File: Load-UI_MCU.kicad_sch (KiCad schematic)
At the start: 30 parts, among them IC1 MSPM0G3519SPMR, IC2 TPS73533DRVT, J1 Conn_01x05_Socket, J10 Conn_01x02_Socket, J11 Conn_01x02_Socket, J15 Conn_01x08_Pin, J8 Conn_01x06_Socket, SW1 SW_Push, SW2 SW_Push, SW3 SW_Push_DPDT

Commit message: Updated schematic and cleaned autosave files
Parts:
- IC1: footprint MSPM03507:QFP50P1200X1200X160-64N -> QFP50P1200X1200X160-64N; symbol MSPM03509-PCB:MSPM0G3507SPMR -> MSPM0G3507SPMR:MSPM0G3507SPMR
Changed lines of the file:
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@@
 	)
 	(symbol
-		(lib_id "MSPM03509-PCB:MSPM0G3507SPMR")
+		(lib_id "MSPM0G3507SPMR:MSPM0G3507SPMR")
 		(at 105.41 81.28 0)
 		(unit 1)
@@
 			)
 		)
-		(property "Footprint" "MSPM03507:QFP50P1200X1200X160-64N"
+		(property "Footprint" "QFP50P1200X1200X160-64N"
 			(at 177.8 143.18 0)
 			(effects

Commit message: Changed NRST button silkscreen
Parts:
- IC1: footprint QFP50P1200X1200X160-64N -> MSPM0SPMR:QFP50P1200X1200X160-64N
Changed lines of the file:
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@@
 			)
 		)
-		(property "Footprint" "QFP50P1200X1200X160-64N"
+		(property "Footprint" "MSPM0SPMR:QFP50P1200X1200X160-64N"
 			(at 177.8 143.18 0)
 			(effects

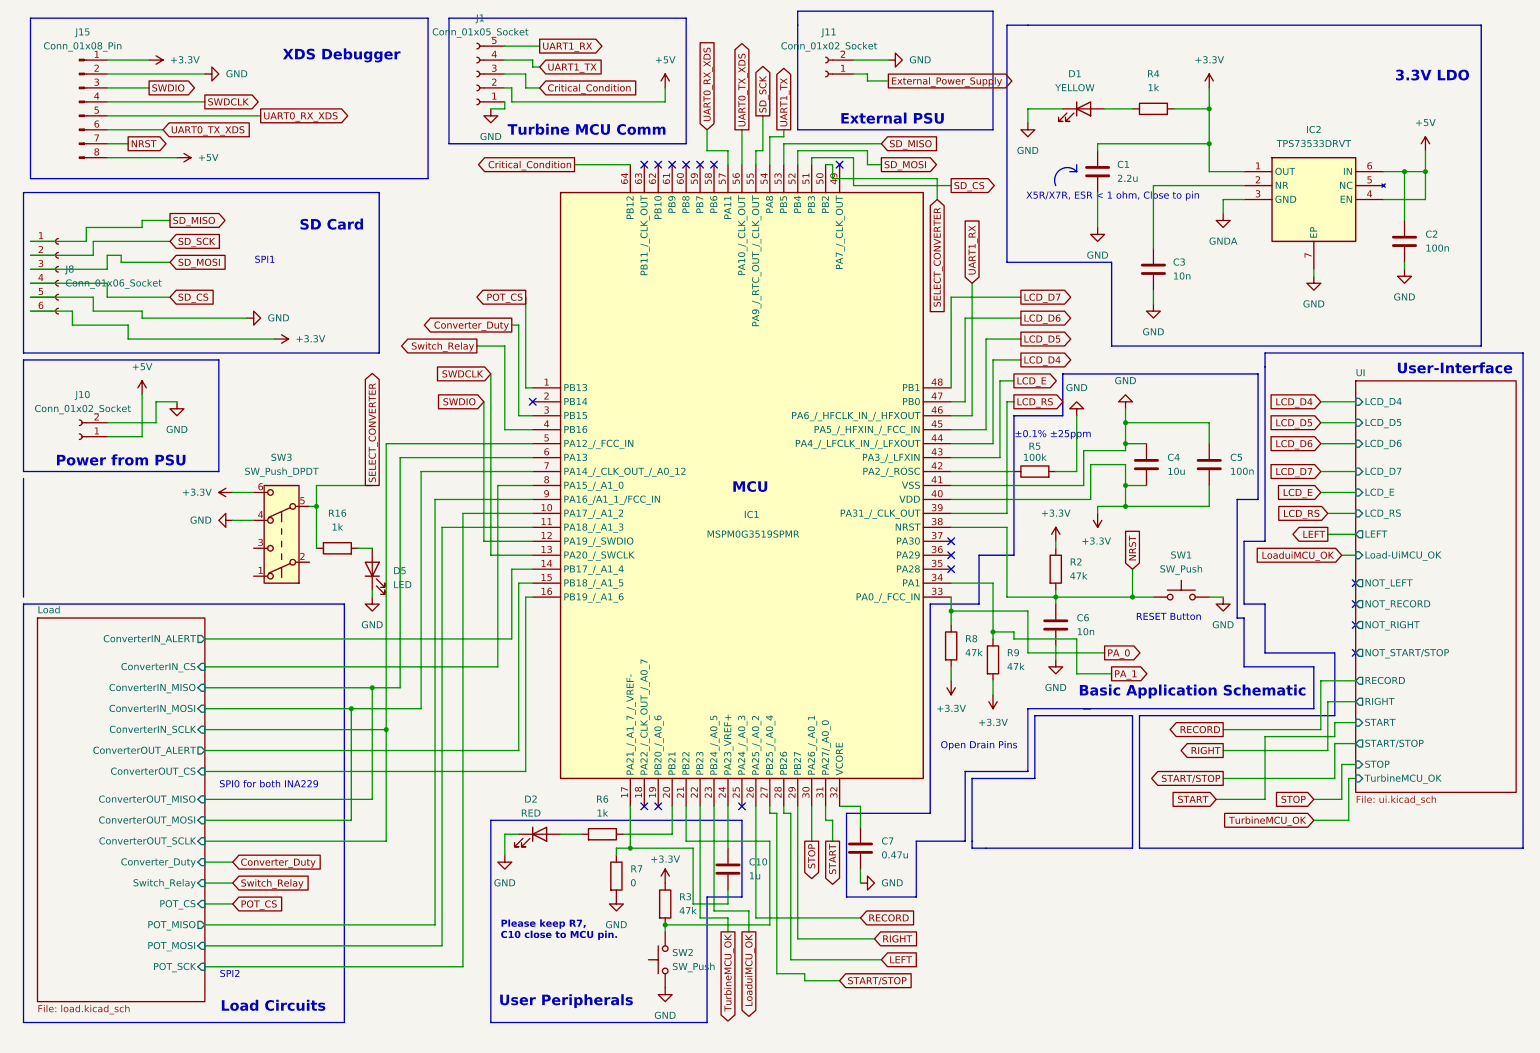
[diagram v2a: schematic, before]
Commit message: Added final changes to PCB: 1. Fixed OV2 ressitors on Power MUX, 2. Added input filtering on both INA229, 3. Changed the LDO layout based on manufacturer recomendations.
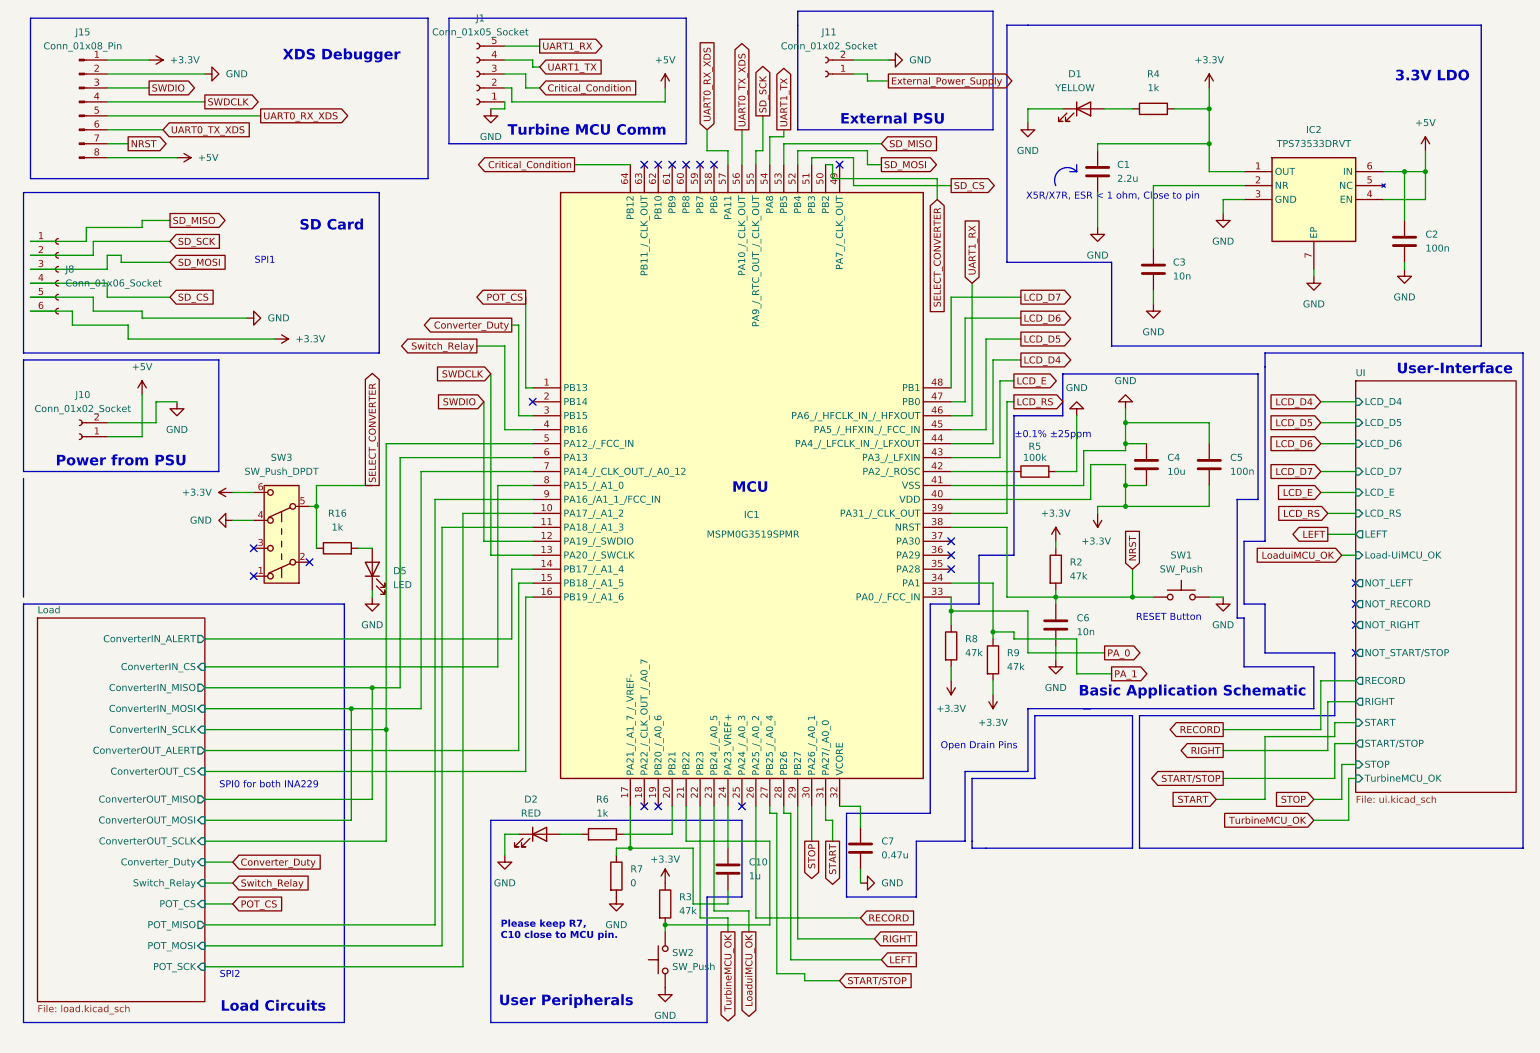
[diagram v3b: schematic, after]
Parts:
- C3: footprint Capacitor_SMD:C_1206_3216Metric_Pad1.33x1.80mm_HandSolder -> Capacitor_SMD:C_0402_1005Metric_Pad0.74x0.62mm_HandSolder
- R4: footprint Resistor_SMD:R_1206_3216Metric_Pad1.30x1.75mm_HandSolder -> Resistor_SMD:R_0805_2012Metric_Pad1.20x1.40mm_HandSolder
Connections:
- net GNDA is gone; now on net GND: IC2.3 (GND)
- no-connect marks 18 -> 21
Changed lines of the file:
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@@
 	)
 	(no_connect
+		(at 54.61 115.57)
+	)
+	(no_connect
 		(at 255.27 120.65)
 	)
 	(no_connect
+		(at 54.61 110.49)
+	)
+	(no_connect
 		(at 255.27 129.54)
 	)
@@
 	)
 	(no_connect
+		(at 64.77 113.03)
+	)
+	(no_connect
 		(at 125.73 40.64)
 	)
@@
 	)
 	(symbol
+		(lib_id "power:GND")
+		(at 231.14 49.53 0)
+		(unit 1)
+		(exclude_from_sim no)
+		(in_bom yes)
+		(on_board yes)
+		(dnp no)
+		(fields_autoplaced yes)
+		(property "Reference" "#PWR03"
+			(at 231.14 55.88 0)
+			(effects
+				(font
+					(size 1.27 1.27)
+				)
+				(hide yes)
+			)
+		)
+		(property "Value" "GND"
+			(at 231.14 54.61 0)
+			(effects
+				(font
+					(size 1.27 1.27)
+				)
+			)
+		)
+		(property "Footprint" ""
+			(at 231.14 49.53 0)
+			(effects
+				(font
+					(size 1.27 1.27)
+				)
+				(hide yes)
+			)
+		)
+		(property "Datasheet" ""
+			(at 231.14 49.53 0)
+			(effects
+				(font
+					(size 1.27 1.27)
+				)
+				(hide yes)
+			)
+		)
+		(property "Description" "Power symbol creates a global label with name \"GND\" , ground"
+			(at 231.14 49.53 0)
+			(effects
+				(font
+					(size 1.27 1.27)
+				)
+				(hide yes)
+			)
+		)
+		(pin "1"
+		)
+		(instances
+			(project "Load-UI_MCU"
+				(path "/526b8b14-d04c-43b9-8d25-bcbd5ccf5c4d"
+					(reference "#PWR03")
+					(unit 1)
+				)
+			)
+		)
+	)
+	(symbol
 		(lib_id "Device:R")
 		(at 218.44 30.48 90)
@@
 			)
 		)
-		(property "Footprint" "Resistor_SMD:R_1206_3216Metric_Pad1.30x1.75mm_HandSolder"
+		(property "Footprint" "Resistor_SMD:R_0805_2012Metric_Pad1.20x1.40mm_HandSolder"
 			(at 218.44 32.258 90)
 			(effects
@@
 	)
 	(symbol
-		(lib_id "power:GNDA")
-		(at 231.14 49.53 0)
-		(unit 1)
-		(exclude_from_sim no)
-		(in_bom yes)
-		(on_board yes)
-		(dnp no)
-		(fields_autoplaced yes)
-		(property "Reference" "#PWR03"
-			(at 231.14 55.88 0)
-			(effects
-				(font
-					(size 1.27 1.27)
-				)
-				(hide yes)
-			)
-		)
-		(property "Value" "GNDA"
-			(at 231.14 54.61 0)
-			(effects
-				(font
-					(size 1.27 1.27)
-				)
-			)
-		)
-		(property "Footprint" ""
-			(at 231.14 49.53 0)
-			(effects
-				(font
-					(size 1.27 1.27)
-				)
-				(hide yes)
-			)
-		)
-		(property "Datasheet" ""
-			(at 231.14 49.53 0)
-			(effects
-				(font
-					(size 1.27 1.27)
-				)
-				(hide yes)
-			)
-		)
-		(property "Description" "Power symbol creates a global label with name \"GNDA\" , analog ground"
-			(at 231.14 49.53 0)
-			(effects
-				(font
-					(size 1.27 1.27)
-				)
-				(hide yes)
-			)
-		)
-		(pin "1"
-		)
-		(instances
-			(project "Load-UI_MCU"
-				(path "/526b8b14-d04c-43b9-8d25-bcbd5ccf5c4d"
-					(reference "#PWR03")
-					(unit 1)
-				)
-			)
-		)
-	)
-	(symbol
 		(lib_id "power:GND")
 		(at 200.66 130.81 0)
@@
 			)
 		)
-		(property "Footprint" "Capacitor_SMD:C_1206_3216Metric_Pad1.33x1.80mm_HandSolder"
+		(property "Footprint" "Capacitor_SMD:C_0402_1005Metric_Pad0.74x0.62mm_HandSolder"
 			(at 219.4052 63.5 0)
 			(effects
@@
 			)
 		)
-		(pin "ConverterIN_MISO" input
+		(pin "ConverterIN_MISO" output
 			(at 45.72 135.89 0)
 			(effects
@@
 			)
 		)
-		(pin "ConverterOUT_MISO" input
+		(pin "ConverterOUT_MISO" output
 			(at 45.72 156.21 0)
 			(effects

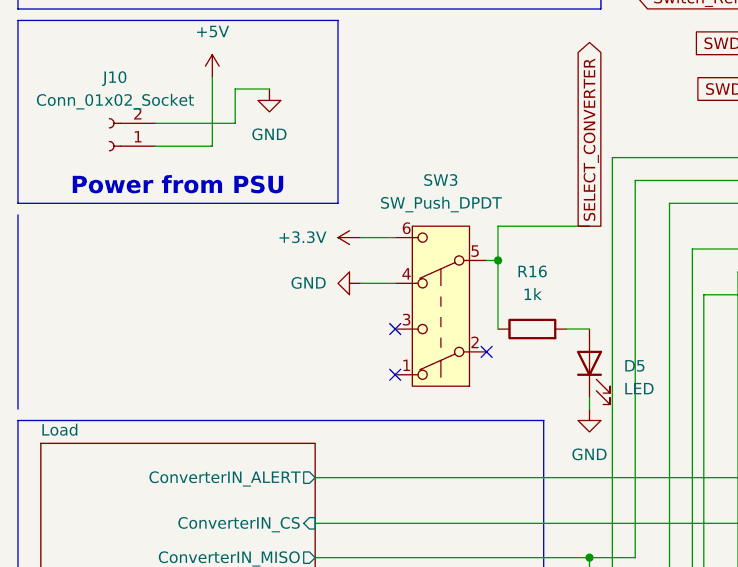
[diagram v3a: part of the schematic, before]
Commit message: Finished pcb for manufacturing, changed some footprints based on what the manufacturer had. Also I fixed the potentiometer footprint.
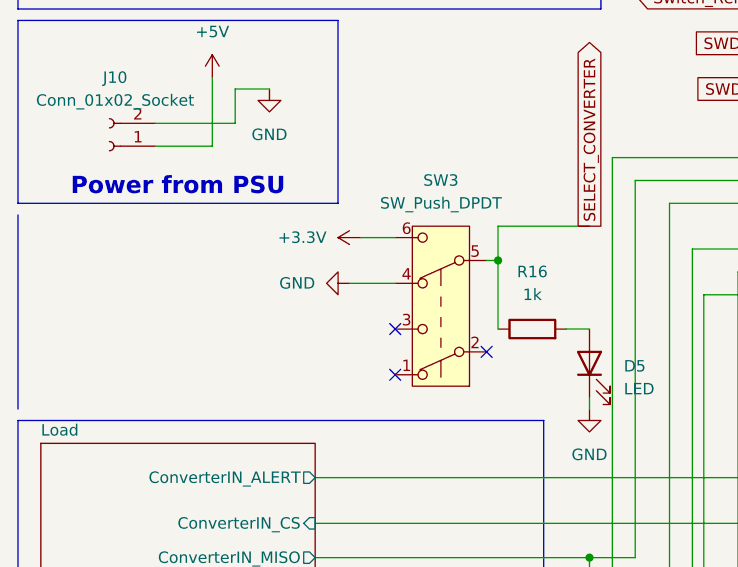
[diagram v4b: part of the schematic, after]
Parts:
- C10: footprint Capacitor_SMD:C_1206_3216Metric_Pad1.33x1.80mm_HandSolder -> Capacitor_SMD:C_0402_1005Metric_Pad0.74x0.62mm_HandSolder
- R7: footprint Resistor_THT:R_Axial_DIN0207_L6.3mm_D2.5mm_P7.62mm_Horizontal -> Resistor_SMD:R_0402_1005Metric_Pad0.72x0.64mm_HandSolder
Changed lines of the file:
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@@
 	(wire
 		(pts
-			(xy 50.8 105.41) (xy 54.61 105.41)
+			(xy 49.53 105.41) (xy 54.61 105.41)
 		)
 		(stroke
@@
 	(symbol
 		(lib_id "power:GND")
-		(at 50.8 105.41 270)
+		(at 49.53 105.41 270)
 		(unit 1)
 		(exclude_from_sim no)
@@
 		(fields_autoplaced yes)
 		(property "Reference" "#PWR082"
-			(at 44.45 105.41 0)
+			(at 43.18 105.41 0)
 			(effects
 				(font
@@
 		)
 		(property "Value" "GND"
-			(at 46.99 105.4099 90)
+			(at 45.72 105.4099 90)
 			(effects
 				(font
@@
 		)
 		(property "Footprint" ""
-			(at 50.8 105.41 0)
+			(at 49.53 105.41 0)
 			(effects
 				(font
@@
 		)
 		(property "Datasheet" ""
-			(at 50.8 105.41 0)
+			(at 49.53 105.41 0)
 			(effects
 				(font
@@
 		)
 		(property "Description" "Power symbol creates a global label with name \"GND\" , ground"
-			(at 50.8 105.41 0)
+			(at 49.53 105.41 0)
 			(effects
 				(font
@@
 			)
 		)
-		(property "Footprint" "Resistor_THT:R_Axial_DIN0207_L6.3mm_D2.5mm_P7.62mm_Horizontal"
+		(property "Footprint" "Resistor_SMD:R_0402_1005Metric_Pad0.72x0.64mm_HandSolder"
 			(at 118.872 170.18 90)
 			(effects
@@
 			)
 		)
-		(property "Footprint" "Capacitor_SMD:C_1206_3216Metric_Pad1.33x1.80mm_HandSolder"
+		(property "Footprint" "Capacitor_SMD:C_0402_1005Metric_Pad0.74x0.62mm_HandSolder"
 			(at 141.9352 172.72 0)
 			(effects

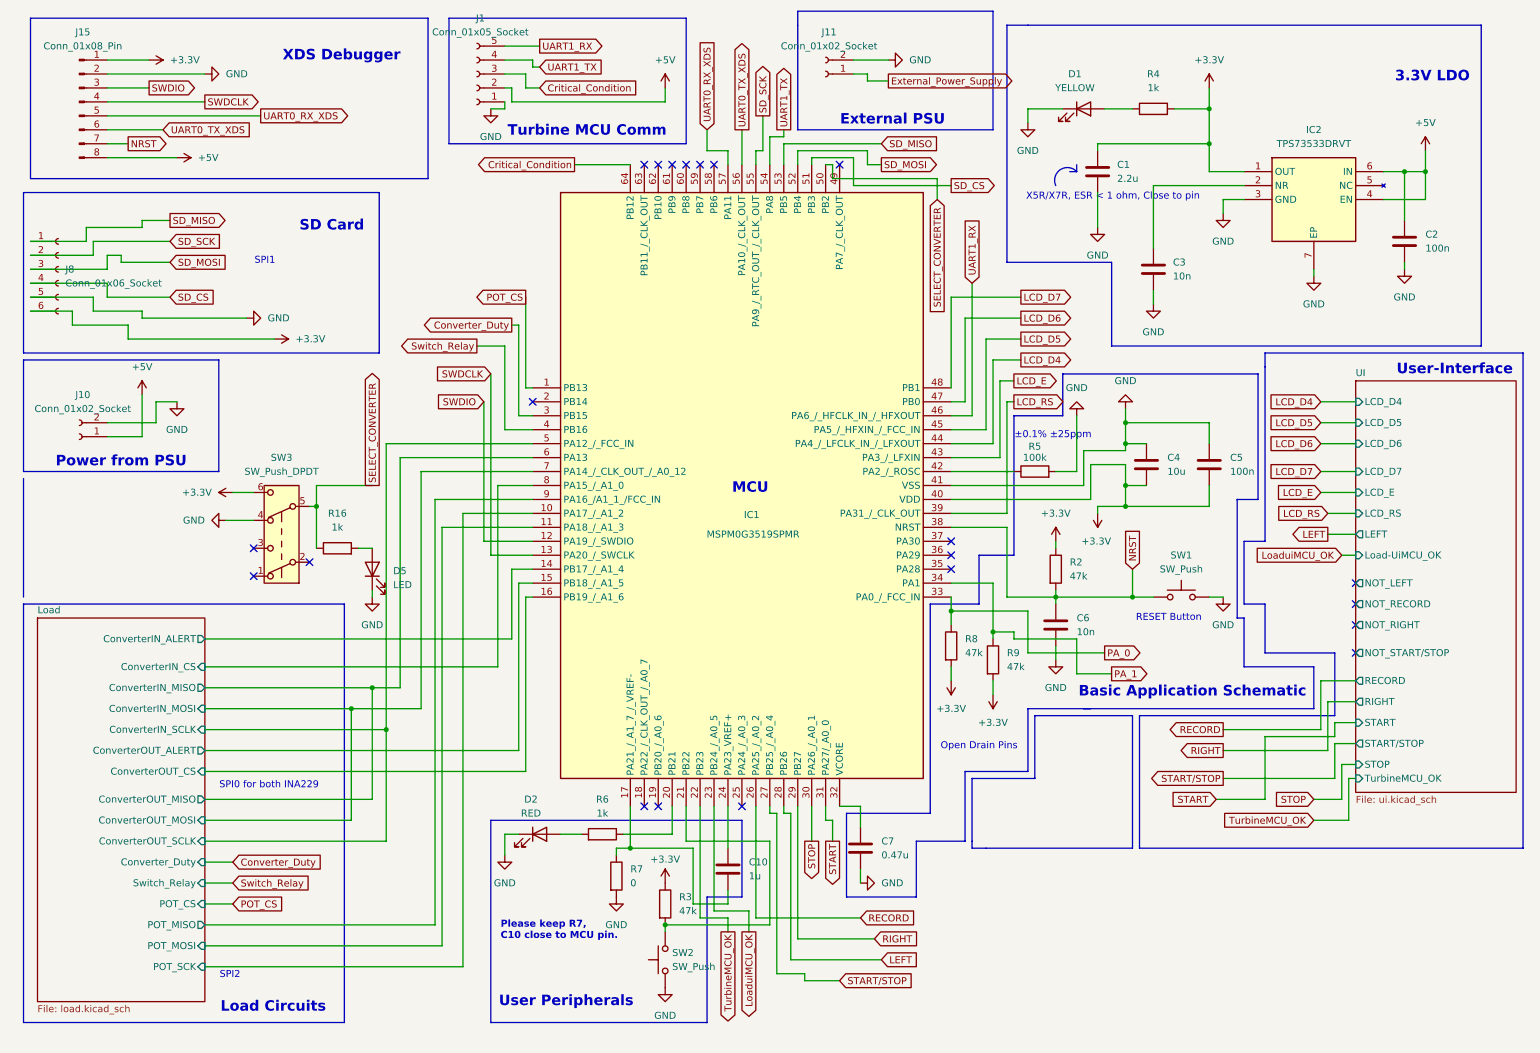
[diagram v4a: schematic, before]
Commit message: Removed unnecessary hex inverter, fixed record button connection, change relay resistors to smd
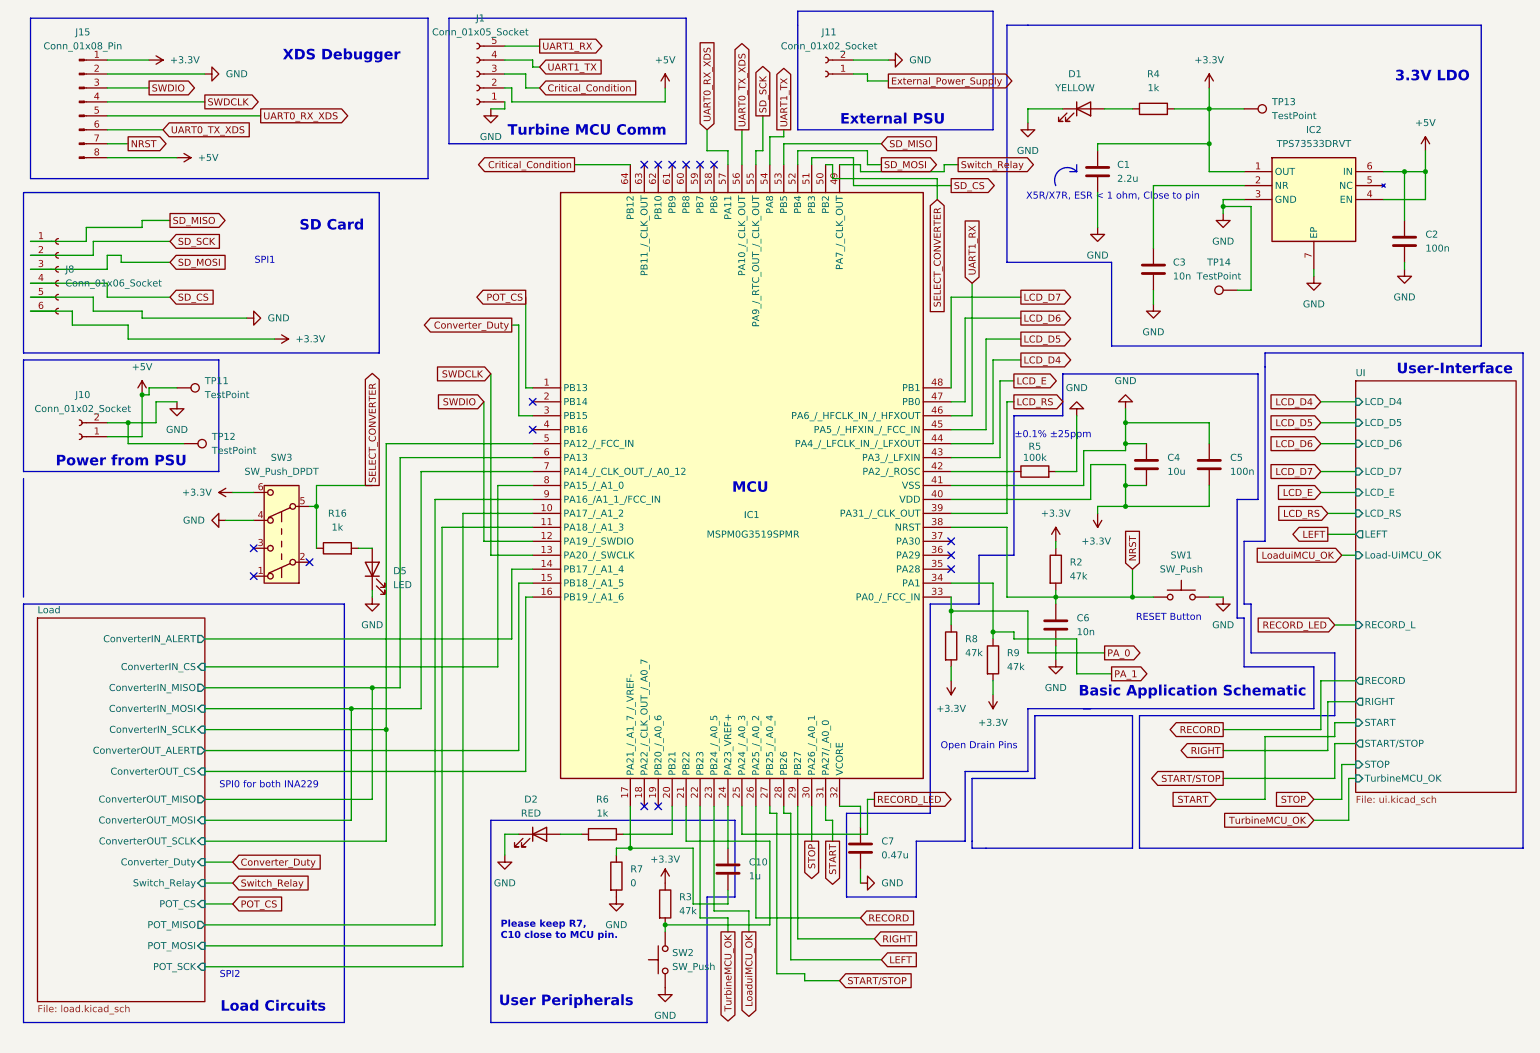
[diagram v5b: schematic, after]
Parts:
- added TP11, TP12, TP13, TP14: TestPoint, TestPoint:TestPoint_Pad_D1.0mm, symbol Connector:TestPoint
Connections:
- net +3.3V: now also TP13.1
- net +5V: now also TP11.1
- net GND: now also TP12.1, TP14.1
- net Switch_Relay: now also IC1.49 (PA7_/_CLK_OUT); no longer IC1.4 (PB16)
- net RECORD_LED: now reaches IC1.25 (PA24_/_A0_3)
- no-connect marks 21 -> 16
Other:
- sheet UI ports: added RECORD_L; removed NOT_LEFT, NOT_RECORD, NOT_RIGHT, NOT_START/STOP
